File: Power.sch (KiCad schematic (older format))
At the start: 0 parts

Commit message: Completed LED Driver Video + Power Module
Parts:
- added C? (x2): C, ~, symbol C
- added F? (x4): FUSE, ~, symbol FUSE
- added L? (x2): INDUCTOR, ~, symbol INDUCTOR
- added P?: CONN_12X2, symbol CONN_12X2
- added R?: R, ~, symbol R
- added SW?: SWITCH_INV, ~, symbol SWITCH_INV
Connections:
- net labels added: +12P, +12V, +3.3V, +5V, -12P, -12V, GND
- wire segments 0 -> 36
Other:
- note added: "CONFIRM DGND AND GND CONNECTIONS BEFORE LAYOUT"

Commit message: Fan Module Update
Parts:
- removed F? (x4): FUSE, ~, symbol FUSE
- added TH? (x4): THERMISTOR, ~, symbol THERMISTOR
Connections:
- net labels added: +12C
- wire segments 36 -> 37
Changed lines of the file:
@@
 	1    0    0    -1
 $EndComp
-Text Notes 1000 2700 0    60   ~ 0
+Text Notes 1050 2350 0    60   ~ 0
 CONFIRM DGND AND GND CONNECTIONS BEFORE LAYOUT
 $Comp
@@
 $EndComp
 $Comp
-L FUSE F?
-U 1 1 52F68298
-P 3700 3350
-F 0 "F?" H 3800 3400 40  0000 C CNN
-F 1 "FUSE" H 3600 3300 40  0000 C CNN
-F 2 "~" H 3700 3350 60  0000 C CNN
-F 3 "~" H 3700 3350 60  0000 C CNN
-	1    3700 3350
-	1    0    0    -1
-$EndComp
-$Comp
-L FUSE F?
-U 1 1 52F682A5
-P 4350 3550
-F 0 "F?" H 4450 3600 40  0000 C CNN
-F 1 "FUSE" H 4250 3500 40  0000 C CNN
-F 2 "~" H 4350 3550 60  0000 C CNN
-F 3 "~" H 4350 3550 60  0000 C CNN
-	1    4350 3550
-	1    0    0    -1
-$EndComp
-$Comp
-L FUSE F?
-U 1 1 52F682AB
-P 5000 3750
-F 0 "F?" H 5100 3800 40  0000 C CNN
-F 1 "FUSE" H 4900 3700 40  0000 C CNN
-F 2 "~" H 5000 3750 60  0000 C CNN
-F 3 "~" H 5000 3750 60  0000 C CNN
-	1    5000 3750
-	1    0    0    -1
-$EndComp
-$Comp
-L FUSE F?
-U 1 1 52F682B1
-P 5700 3950
-F 0 "F?" H 5800 4000 40  0000 C CNN
-F 1 "FUSE" H 5600 3900 40  0000 C CNN
-F 2 "~" H 5700 3950 60  0000 C CNN
-F 3 "~" H 5700 3950 60  0000 C CNN
-	1    5700 3950
-	1    0    0    -1
-$EndComp
-$Comp
 L SWITCH_INV SW?
 U 1 1 52F682B9
@@
 Wire Wire Line
 	10450 3650 10450 3450
+$Comp
+L +12C #PWR?
+U 1 1 52FA4EC0
+P 3250 2750
+F 0 "#PWR?" H 3250 2720 30  0001 C CNN
+F 1 "+12C" H 3250 2860 40  0000 C CNN
+F 2 "" H 3250 2750 60  0000 C CNN
+F 3 "" H 3250 2750 60  0000 C CNN
+	1    3250 2750
+	1    0    0    -1
+$EndComp
+Wire Wire Line
+	3250 2750 3250 3750
+Connection ~ 3250 3750
+$Comp
+L THERMISTOR TH?
+U 1 1 52FA5A15
+P 3700 3350
+F 0 "TH?" V 3800 3400 50  0000 C CNN
+F 1 "THERMISTOR" V 3600 3350 50  0000 C CNN
+F 2 "~" H 3700 3350 60  0000 C CNN
+F 3 "~" H 3700 3350 60  0000 C CNN
+	1    3700 3350
+	0    -1   -1   0
+$EndComp
+$Comp
+L THERMISTOR TH?
+U 1 1 52FA5A22
+P 4350 3550
+F 0 "TH?" V 4450 3600 50  0000 C CNN
+F 1 "THERMISTOR" V 4250 3550 50  0000 C CNN
+F 2 "~" H 4350 3550 60  0000 C CNN
+F 3 "~" H 4350 3550 60  0000 C CNN
+	1    4350 3550
+	0    -1   -1   0
+$EndComp
+$Comp
+L THERMISTOR TH?
+U 1 1 52FA5A28
+P 5000 3750
+F 0 "TH?" V 5100 3800 50  0000 C CNN
+F 1 "THERMISTOR" V 4900 3750 50  0000 C CNN
+F 2 "~" H 5000 3750 60  0000 C CNN
+F 3 "~" H 5000 3750 60  0000 C CNN
+	1    5000 3750
+	0    -1   -1   0
+$EndComp
+$Comp
+L THERMISTOR TH?
+U 1 1 52FA5A2E
+P 5700 3950
+F 0 "TH?" V 5800 4000 50  0000 C CNN
+F 1 "THERMISTOR" V 5600 3950 50  0000 C CNN
+F 2 "~" H 5700 3950 60  0000 C CNN
+F 3 "~" H 5700 3950 60  0000 C CNN
+	1    5700 3950
+	0    -1   -1   0
+$EndComp
 $EndSCHEMATC

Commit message: Started Layout Outline.  Completed other schem videos
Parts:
- added C?: C, ~, symbol C
- added L?: INDUCTOR, ~, symbol INDUCTOR
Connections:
- net +3.3V: no longer TH?.2
- net +5V: now also C?.1, L?.2; no longer TH?.2
- net GND: now also C?.2
- new net +3.3VP: TH?.2
- new net +5P: L?.1, TH?.2
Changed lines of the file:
@@
 $Descr A4 11693 8268
 encoding utf-8
-Sheet 4 9
+Sheet 3 9
 Title ""
-Date "11 feb 2014"
+Date "17 feb 2014"
 Rev ""
 Comp ""
@@
 L +5V #PWR?
 U 1 1 52F67F60
-P 5250 2750
-F 0 "#PWR?" H 5250 2840 20  0001 C CNN
-F 1 "+5V" H 5250 2840 30  0000 C CNN
-F 2 "" H 5250 2750 60  0000 C CNN
-F 3 "" H 5250 2750 60  0000 C CNN
-	1    5250 2750
-	1    0    0    -1
-$EndComp
-$Comp
-L +3.3V #PWR?
-U 1 1 52F68100
-P 4650 2750
-F 0 "#PWR?" H 4650 2710 30  0001 C CNN
-F 1 "+3.3V" H 4650 2860 30  0000 C CNN
-F 2 "" H 4650 2750 60  0000 C CNN
-F 3 "" H 4650 2750 60  0000 C CNN
-	1    4650 2750
+P 10450 2000
+F 0 "#PWR?" H 10450 2090 20  0001 C CNN
+F 1 "+5V" H 10450 2090 30  0000 C CNN
+F 2 "" H 10450 2000 60  0000 C CNN
+F 3 "" H 10450 2000 60  0000 C CNN
+	1    10450 2000
 	1    0    0    -1
 $EndComp
@@
 	9750 5050 9750 4950
 Wire Wire Line
-	9750 4550 9750 4150
+	9750 4150 9750 4550
 Wire Wire Line
 	9150 3650 10450 3650
@@
 	0    -1   -1   0
 $EndComp
+$Comp
+L +5P #PWR?
+U 1 1 530231B7
+P 5250 2750
+F 0 "#PWR?" H 5250 2880 20  0001 C CNN
+F 1 "+5P" H 5250 2850 30  0000 C CNN
+F 2 "" H 5250 2750 60  0000 C CNN
+F 3 "" H 5250 2750 60  0000 C CNN
+	1    5250 2750
+	1    0    0    -1
+$EndComp
+$Comp
+L +5P #PWR?
+U 1 1 530231D8
+P 8050 2000
+F 0 "#PWR?" H 8050 2130 20  0001 C CNN
+F 1 "+5P" H 8050 2100 30  0000 C CNN
+F 2 "" H 8050 2000 60  0000 C CNN
+F 3 "" H 8050 2000 60  0000 C CNN
+	1    8050 2000
+	1    0    0    -1
+$EndComp
+$Comp
+L INDUCTOR L?
+U 1 1 530231DE
+P 8850 2300
+F 0 "L?" V 8800 2300 40  0000 C CNN
+F 1 "INDUCTOR" V 8950 2300 40  0000 C CNN
+F 2 "~" H 8850 2300 60  0000 C CNN
+F 3 "~" H 8850 2300 60  0000 C CNN
+	1    8850 2300
+	0    -1   -1   0
+$EndComp
+$Comp
+L C C?
+U 1 1 530231E4
+P 9750 2600
+F 0 "C?" H 9750 2700 40  0000 L CNN
+F 1 "C" H 9756 2515 40  0000 L CNN
+F 2 "~" H 9788 2450 30  0000 C CNN
+F 3 "~" H 9750 2600 60  0000 C CNN
+	1    9750 2600
+	1    0    0    -1
+$EndComp
+Wire Wire Line
+	9150 2300 10450 2300
+$Comp
+L GND #PWR?
+U 1 1 530231EC
+P 9750 3150
+F 0 "#PWR?" H 9750 3150 30  0001 C CNN
+F 1 "GND" H 9750 3080 30  0001 C CNN
+F 2 "" H 9750 3150 60  0000 C CNN
+F 3 "" H 9750 3150 60  0000 C CNN
+	1    9750 3150
+	1    0    0    -1
+$EndComp
+Wire Wire Line
+	9750 2800 9750 3150
+Wire Wire Line
+	8550 2300 8050 2300
+Connection ~ 9750 2300
+Wire Wire Line
+	9750 2300 9750 2400
+Wire Wire Line
+	10450 2300 10450 2000
+Wire Wire Line
+	8050 2300 8050 2000
+$Comp
+L +3.3VP #PWR?
+U 1 1 53023523
+P 4650 2750
+F 0 "#PWR?" H 4700 2780 20  0001 C CNN
+F 1 "+3.3VP" H 4650 2840 30  0000 C CNN
+F 2 "" H 4650 2750 60  0000 C CNN
+F 3 "" H 4650 2750 60  0000 C CNN
+	1    4650 2750
+	1    0    0    -1
+$EndComp
 $EndSCHEMATC

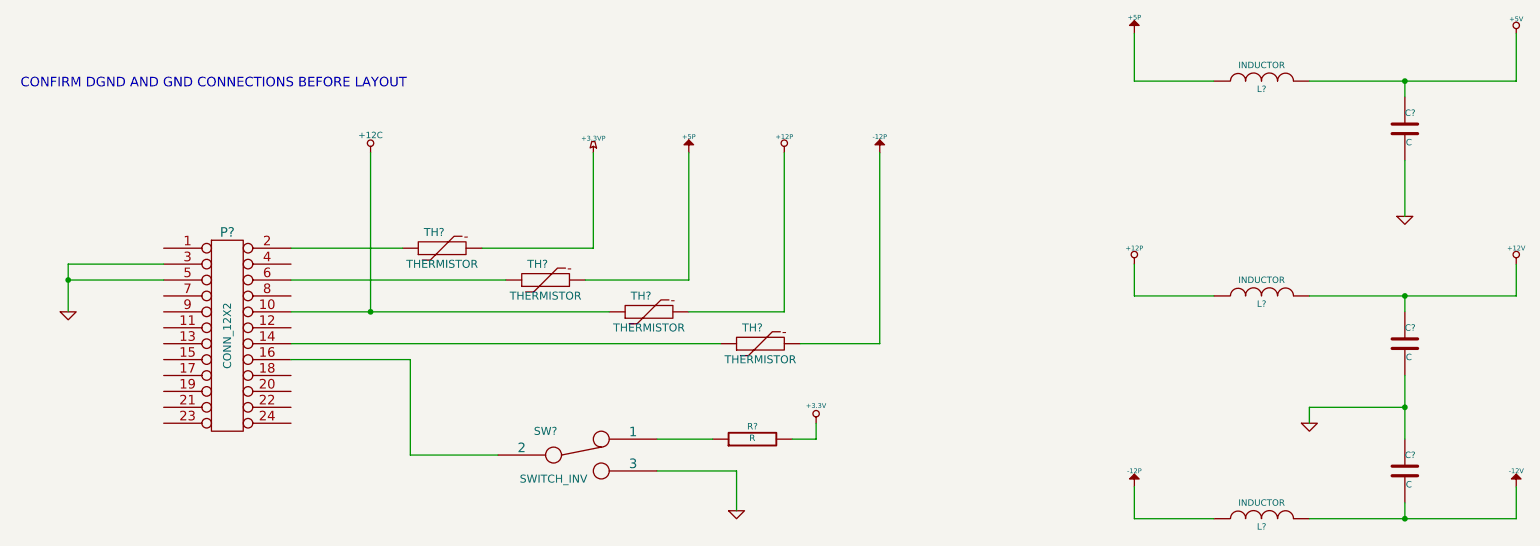
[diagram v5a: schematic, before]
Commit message: started associating relay parts
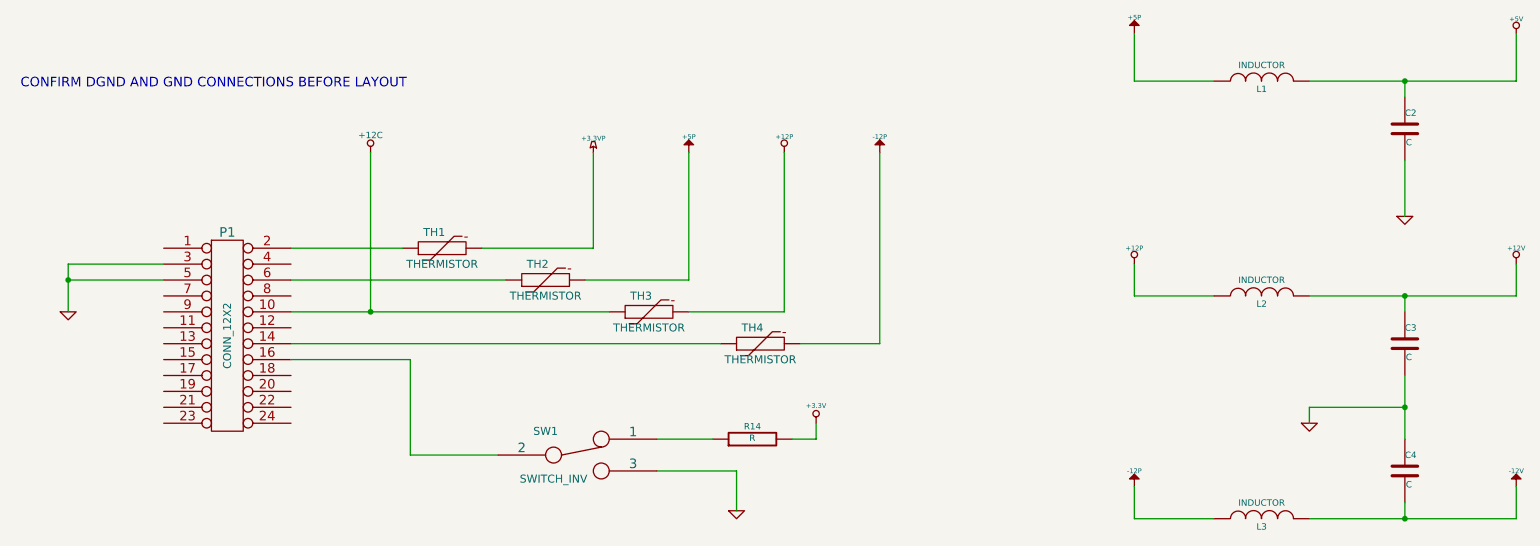
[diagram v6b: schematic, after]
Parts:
- gave numbers to parts that had none: 13
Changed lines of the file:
@@
 Sheet 3 9
 Title ""
-Date "17 feb 2014"
+Date "20 feb 2014"
 Rev ""
 Comp ""
@@
 $EndDescr
 $Comp
-L CONN_12X2 P?
+L CONN_12X2 P1
 U 1 1 52F67DB2
 P 2350 3900
-F 0 "P?" H 2350 4550 60  0000 C CNN
+F 0 "P1" H 2350 4550 60  0000 C CNN
 F 1 "CONN_12X2" V 2350 3900 50  0000 C CNN
 F 2 "" H 2350 3900 60  0000 C CNN
@@
 $EndComp
 $Comp
-L +3.3V #PWR?
+L +3.3V #PWR010
 U 1 1 52F67DC1
 P 6050 4450
-F 0 "#PWR?" H 6050 4410 30  0001 C CNN
+F 0 "#PWR010" H 6050 4410 30  0001 C CNN
 F 1 "+3.3V" H 6050 4560 30  0000 C CNN
 F 2 "" H 6050 4450 60  0000 C CNN
@@
 $EndComp
 $Comp
-L GND #PWR?
+L GND #PWR011
 U 1 1 52F67DD1
 P 1350 3750
-F 0 "#PWR?" H 1350 3750 30  0001 C CNN
+F 0 "#PWR011" H 1350 3750 30  0001 C CNN
 F 1 "GND" H 1350 3680 30  0001 C CNN
 F 2 "" H 1350 3750 60  0000 C CNN
@@
 CONFIRM DGND AND GND CONNECTIONS BEFORE LAYOUT
 $Comp
-L +5V #PWR?
+L +5V #PWR012
 U 1 1 52F67F60
 P 10450 2000
-F 0 "#PWR?" H 10450 2090 20  0001 C CNN
+F 0 "#PWR012" H 10450 2090 20  0001 C CNN
 F 1 "+5V" H 10450 2090 30  0000 C CNN
 F 2 "" H 10450 2000 60  0000 C CNN
@@
 $EndComp
 $Comp
-L SWITCH_INV SW?
+L SWITCH_INV SW1
 U 1 1 52F682B9
 P 4550 4650
-F 0 "SW?" H 4350 4800 50  0000 C CNN
+F 0 "SW1" H 4350 4800 50  0000 C CNN
 F 1 "SWITCH_INV" H 4400 4500 50  0000 C CNN
 F 2 "~" H 4550 4650 60  0000 C CNN
@@
 $EndComp
 $Comp
-L +12P #PWR?
+L +12P #PWR013
 U 1 1 52F682C8
 P 5850 2750
-F 0 "#PWR?" H 5850 2720 30  0001 C CNN
+F 0 "#PWR013" H 5850 2720 30  0001 C CNN
 F 1 "+12P" H 5850 2850 30  0000 C CNN
 F 2 "" H 5850 2750 60  0000 C CNN
@@
 $EndComp
 $Comp
-L -12P #PWR?
+L -12P #PWR014
 U 1 1 52F68B13
 P 6450 2750
-F 0 "#PWR?" H 6450 2880 20  0001 C CNN
+F 0 "#PWR014" H 6450 2880 20  0001 C CNN
 F 1 "-12P" H 6450 2850 30  0000 C CNN
 F 2 "" H 6450 2750 60  0000 C CNN
@@
 	3500 4050 2750 4050
 $Comp
-L GND #PWR?
+L GND #PWR015
 U 1 1 52F68F28
 P 5550 5000
-F 0 "#PWR?" H 5550 5000 30  0001 C CNN
+F 0 "#PWR015" H 5550 5000 30  0001 C CNN
 F 1 "GND" H 5550 4930 30  0001 C CNN
 F 2 "" H 5550 5000 60  0000 C CNN
@@
 	5550 4750 5550 5000
 $Comp
-L R R?
+L R R14
 U 1 1 52F68F4E
 P 5650 4550
-F 0 "R?" V 5730 4550 40  0000 C CNN
+F 0 "R14" V 5730 4550 40  0000 C CNN
 F 1 "R" V 5657 4551 40  0000 C CNN
 F 2 "~" V 5580 4550 30  0000 C CNN
@@
 	6050 4550 6050 4450
 $Comp
-L +12P #PWR?
+L +12P #PWR016
 U 1 1 52F68F88
 P 8050 3450
-F 0 "#PWR?" H 8050 3420 30  0001 C CNN
+F 0 "#PWR016" H 8050 3420 30  0001 C CNN
 F 1 "+12P" H 8050 3550 30  0000 C CNN
 F 2 "" H 8050 3450 60  0000 C CNN
@@
 $EndComp
 $Comp
-L -12P #PWR?
+L -12P #PWR017
 U 1 1 52F68F8E
 P 8050 4850
-F 0 "#PWR?" H 8050 4980 20  0001 C CNN
+F 0 "#PWR017" H 8050 4980 20  0001 C CNN
 F 1 "-12P" H 8050 4950 30  0000 C CNN
 F 2 "" H 8050 4850 60  0000 C CNN
@@
 $EndComp
 $Comp
-L INDUCTOR L?
+L INDUCTOR L2
 U 1 1 52F68FA0
 P 8850 3650
-F 0 "L?" V 8800 3650 40  0000 C CNN
+F 0 "L2" V 8800 3650 40  0000 C CNN
 F 1 "INDUCTOR" V 8950 3650 40  0000 C CNN
 F 2 "~" H 8850 3650 60  0000 C CNN
@@
 $EndComp
 $Comp
-L INDUCTOR L?
+L INDUCTOR L3
 U 1 1 52F68FAD
 P 8850 5050
-F 0 "L?" V 8800 5050 40  0000 C CNN
+F 0 "L3" V 8800 5050 40  0000 C CNN
 F 1 "INDUCTOR" V 8950 5050 40  0000 C CNN
 F 2 "~" H 8850 5050 60  0000 C CNN
@@
 $EndComp
 $Comp
-L C C?
+L C C3
 U 1 1 52F68FC9
 P 9750 3950
-F 0 "C?" H 9750 4050 40  0000 L CNN
+F 0 "C3" H 9750 4050 40  0000 L CNN
 F 1 "C" H 9756 3865 40  0000 L CNN
 F 2 "~" H 9788 3800 30  0000 C CNN
@@
 $EndComp
 $Comp
-L C C?
+L C C4
 U 1 1 52F68FD6
 P 9750 4750
-F 0 "C?" H 9750 4850 40  0000 L CNN
+F 0 "C4" H 9750 4850 40  0000 L CNN
 F 1 "C" H 9756 4665 40  0000 L CNN
 F 2 "~" H 9788 4600 30  0000 C CNN
@@
 	9150 3650 10450 3650
 $Comp
-L GND #PWR?
+L GND #PWR018
 U 1 1 52F6902C
 P 9150 4450
-F 0 "#PWR?" H 9150 4450 30  0001 C CNN
+F 0 "#PWR018" H 9150 4450 30  0001 C CNN
 F 1 "GND" H 9150 4380 30  0001 C CNN
 F 2 "" H 9150 4450 60  0000 C CNN
@@
 	8050 3650 8050 3450
 $Comp
-L +12V #PWR?
+L +12V #PWR019
 U 1 1 52F690A0
 P 10450 3450
-F 0 "#PWR?" H 10450 3400 20  0001 C CNN
+F 0 "#PWR019" H 10450 3400 20  0001 C CNN
 F 1 "+12V" H 10450 3550 30  0000 C CNN
 F 2 "" H 10450 3450 60  0000 C CNN
@@
 Connection ~ 9750 3650
 $Comp
-L -12V #PWR?
+L -12V #PWR020
 U 1 1 52F690D4
 P 10450 4850
-F 0 "#PWR?" H 10450 4980 20  0001 C CNN
+F 0 "#PWR020" H 10450 4980 20  0001 C CNN
 F 1 "-12V" H 10450 4950 30  0000 C CNN
 F 2 "" H 10450 4850 60  0000 C CNN
@@
 	10450 3650 10450 3450
 $Comp
-L +12C #PWR?
+L +12C #PWR021
 U 1 1 52FA4EC0
 P 3250 2750
-F 0 "#PWR?" H 3250 2720 30  0001 C CNN
+F 0 "#PWR021" H 3250 2720 30  0001 C CNN
 F 1 "+12C" H 3250 2860 40  0000 C CNN
 F 2 "" H 3250 2750 60  0000 C CNN
@@
 Connection ~ 3250 3750
 $Comp
-L THERMISTOR TH?
+L THERMISTOR TH1
 U 1 1 52FA5A15
 P 3700 3350
-F 0 "TH?" V 3800 3400 50  0000 C CNN
+F 0 "TH1" V 3800 3400 50  0000 C CNN
 F 1 "THERMISTOR" V 3600 3350 50  0000 C CNN
 F 2 "~" H 3700 3350 60  0000 C CNN
@@
 $EndComp
 $Comp
-L THERMISTOR TH?
+L THERMISTOR TH2
 U 1 1 52FA5A22
 P 4350 3550
-F 0 "TH?" V 4450 3600 50  0000 C CNN
+F 0 "TH2" V 4450 3600 50  0000 C CNN
 F 1 "THERMISTOR" V 4250 3550 50  0000 C CNN
 F 2 "~" H 4350 3550 60  0000 C CNN
@@
 $EndComp
 $Comp
-L THERMISTOR TH?
+L THERMISTOR TH3
 U 1 1 52FA5A28
 P 5000 3750
-F 0 "TH?" V 5100 3800 50  0000 C CNN
+F 0 "TH3" V 5100 3800 50  0000 C CNN
 F 1 "THERMISTOR" V 4900 3750 50  0000 C CNN
 F 2 "~" H 5000 3750 60  0000 C CNN
@@
 $EndComp
 $Comp
-L THERMISTOR TH?
+L THERMISTOR TH4
 U 1 1 52FA5A2E
 P 5700 3950
-F 0 "TH?" V 5800 4000 50  0000 C CNN
+F 0 "TH4" V 5800 4000 50  0000 C CNN
 F 1 "THERMISTOR" V 5600 3950 50  0000 C CNN
 F 2 "~" H 5700 3950 60  0000 C CNN
@@
 $EndComp
 $Comp
-L +5P #PWR?
+L +5P #PWR13
 U 1 1 530231B7
 P 5250 2750
-F 0 "#PWR?" H 5250 2880 20  0001 C CNN
+F 0 "#PWR13" H 5250 2880 20  0001 C CNN
 F 1 "+5P" H 5250 2850 30  0000 C CNN
 F 2 "" H 5250 2750 60  0000 C CNN
@@
 $EndComp
 $Comp
-L +5P #PWR?
+L +5P #PWR18
 U 1 1 530231D8
 P 8050 2000
-F 0 "#PWR?" H 8050 2130 20  0001 C CNN
+F 0 "#PWR18" H 8050 2130 20  0001 C CNN
 F 1 "+5P" H 8050 2100 30  0000 C CNN
 F 2 "" H 8050 2000 60  0000 C CNN
@@
 $EndComp
 $Comp
-L INDUCTOR L?
+L INDUCTOR L1
 U 1 1 530231DE
 P 8850 2300
-F 0 "L?" V 8800 2300 40  0000 C CNN
+F 0 "L1" V 8800 2300 40  0000 C CNN
 F 1 "INDUCTOR" V 8950 2300 40  0000 C CNN
 F 2 "~" H 8850 2300 60  0000 C CNN
@@
 $EndComp
 $Comp
-L C C?
+L C C2
 U 1 1 530231E4
 P 9750 2600
-F 0 "C?" H 9750 2700 40  0000 L CNN
+F 0 "C2" H 9750 2700 40  0000 L CNN
 F 1 "C" H 9756 2515 40  0000 L CNN
 F 2 "~" H 9788 2450 30  0000 C CNN
@@
 	9150 2300 10450 2300
 $Comp
-L GND #PWR?
+L GND #PWR022
 U 1 1 530231EC
 P 9750 3150
-F 0 "#PWR?" H 9750 3150 30  0001 C CNN
+F 0 "#PWR022" H 9750 3150 30  0001 C CNN
 F 1 "GND" H 9750 3080 30  0001 C CNN
 F 2 "" H 9750 3150 60  0000 C CNN
@@
 	8050 2300 8050 2000
 $Comp
-L +3.3VP #PWR?
+L +3.3VP #PWR023
 U 1 1 53023523
 P 4650 2750
-F 0 "#PWR?" H 4700 2780 20  0001 C CNN
+F 0 "#PWR023" H 4700 2780 20  0001 C CNN
 F 1 "+3.3VP" H 4650 2840 30  0000 C CNN
 F 2 "" H 4650 2750 60  0000 C CNN

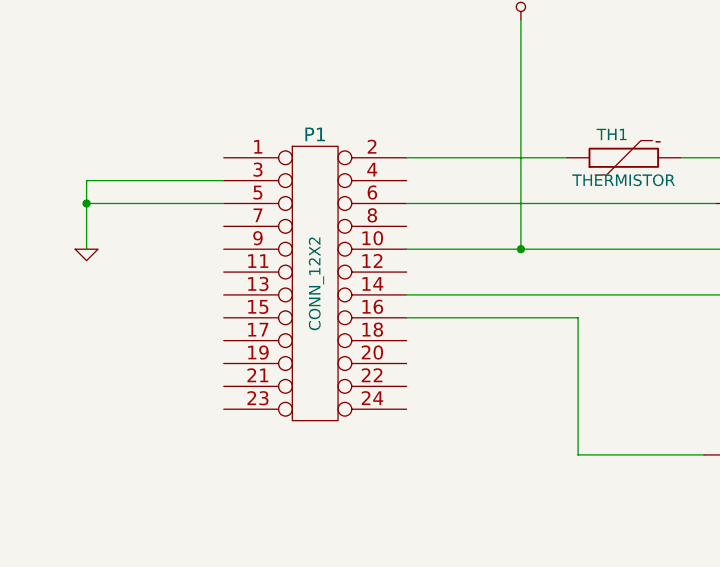
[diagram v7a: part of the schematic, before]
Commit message: Completed terminal block placement and footprints
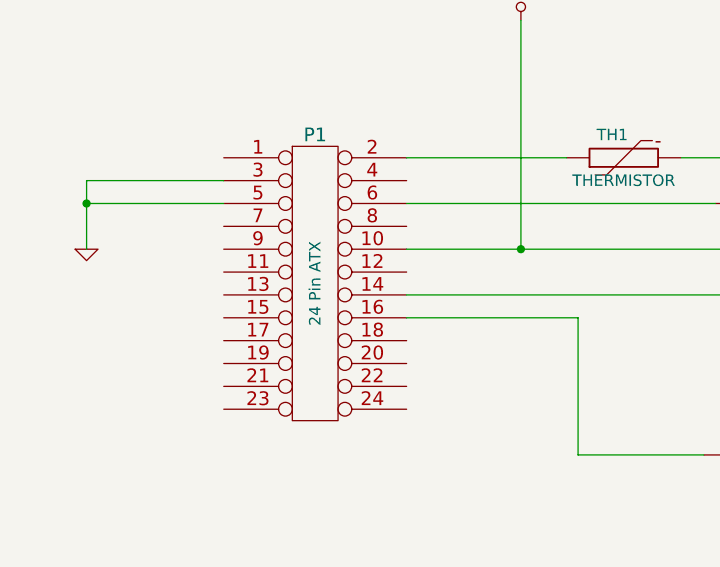
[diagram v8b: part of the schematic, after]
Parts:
- P1: value CONN_12X2 -> 24 Pin ATX; MFG Name (none) -> Molex; Part Number (none) -> 39-30-1240
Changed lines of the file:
@@
 Sheet 3 9
 Title ""
-Date "23 feb 2014"
+Date "2 mar 2014"
 Rev ""
 Comp ""
@@
 P 2350 3900
 F 0 "P1" H 2350 4550 60  0000 C CNN
-F 1 "CONN_12X2" V 2350 3900 50  0000 C CNN
+F 1 "24 Pin ATX" V 2350 3900 50  0000 C CNN
 F 2 "" H 2350 3900 60  0000 C CNN
 F 3 "" H 2350 3900 60  0000 C CNN
+F 4 "39-30-1240" H 2350 3900 60  0001 C CNN "Part Number"
+F 5 "Molex" H 2350 3900 60  0001 C CNN "MFG Name"
 	1    2350 3900
 	1    0    0    -1
 $EndComp
 $Comp
-L +3.3V #PWR27
+L +3.3V #PWR021
 U 1 1 52F67DC1
 P 6050 4450
-F 0 "#PWR27" H 6050 4410 30  0001 C CNN
+F 0 "#PWR021" H 6050 4410 30  0001 C CNN
 F 1 "+3.3V" H 6050 4560 30  0000 C CNN
 F 2 "" H 6050 4450 60  0000 C CNN
@@
 $EndComp
 $Comp
-L GND #PWR21
+L GND #PWR022
 U 1 1 52F67DD1
 P 1350 3750
-F 0 "#PWR21" H 1350 3750 30  0001 C CNN
+F 0 "#PWR022" H 1350 3750 30  0001 C CNN
 F 1 "GND" H 1350 3680 30  0001 C CNN
 F 2 "" H 1350 3750 60  0000 C CNN
@@
 CONFIRM DGND AND GND CONNECTIONS BEFORE LAYOUT
 $Comp
-L +5V #PWR34
+L +5V #PWR023
 U 1 1 52F67F60
 P 10450 2000
-F 0 "#PWR34" H 10450 2090 20  0001 C CNN
+F 0 "#PWR023" H 10450 2090 20  0001 C CNN
 F 1 "+5V" H 10450 2090 30  0000 C CNN
 F 2 "" H 10450 2000 60  0000 C CNN
@@
 $EndComp
 $Comp
-L +12P #PWR26
+L +12P #PWR024
 U 1 1 52F682C8
 P 5850 2750
-F 0 "#PWR26" H 5850 2720 30  0001 C CNN
+F 0 "#PWR024" H 5850 2720 30  0001 C CNN
 F 1 "+12P" H 5850 2850 30  0000 C CNN
 F 2 "" H 5850 2750 60  0000 C CNN
@@
 $EndComp
 $Comp
-L -12P #PWR28
+L -12P #PWR025
 U 1 1 52F68B13
 P 6450 2750
-F 0 "#PWR28" H 6450 2880 20  0001 C CNN
+F 0 "#PWR025" H 6450 2880 20  0001 C CNN
 F 1 "-12P" H 6450 2850 30  0000 C CNN
 F 2 "" H 6450 2750 60  0000 C CNN
@@
 	3500 4050 2750 4050
 $Comp
-L GND #PWR25
+L GND #PWR026
 U 1 1 52F68F28
 P 5550 5000
-F 0 "#PWR25" H 5550 5000 30  0001 C CNN
+F 0 "#PWR026" H 5550 5000 30  0001 C CNN
 F 1 "GND" H 5550 4930 30  0001 C CNN
 F 2 "" H 5550 5000 60  0000 C CNN
@@
 	6050 4550 6050 4450
 $Comp
-L +12P #PWR30
+L +12P #PWR027
 U 1 1 52F68F88
 P 8050 3450
-F 0 "#PWR30" H 8050 3420 30  0001 C CNN
+F 0 "#PWR027" H 8050 3420 30  0001 C CNN
 F 1 "+12P" H 8050 3550 30  0000 C CNN
 F 2 "" H 8050 3450 60  0000 C CNN
@@
 $EndComp
 $Comp
-L -12P #PWR31
+L -12P #PWR028
 U 1 1 52F68F8E
 P 8050 4850
-F 0 "#PWR31" H 8050 4980 20  0001 C CNN
+F 0 "#PWR028" H 8050 4980 20  0001 C CNN
 F 1 "-12P" H 8050 4950 30  0000 C CNN
 F 2 "" H 8050 4850 60  0000 C CNN
@@
 	9150 3650 10450 3650
 $Comp
-L GND #PWR32
+L GND #PWR029
 U 1 1 52F6902C
 P 9150 4450
-F 0 "#PWR32" H 9150 4450 30  0001 C CNN
+F 0 "#PWR029" H 9150 4450 30  0001 C CNN
 F 1 "GND" H 9150 4380 30  0001 C CNN
 F 2 "" H 9150 4450 60  0000 C CNN
@@
 	8050 3650 8050 3450
 $Comp
-L +12V #PWR35
+L +12V #PWR030
 U 1 1 52F690A0
 P 10450 3450
-F 0 "#PWR35" H 10450 3400 20  0001 C CNN
+F 0 "#PWR030" H 10450 3400 20  0001 C CNN
 F 1 "+12V" H 10450 3550 30  0000 C CNN
 F 2 "" H 10450 3450 60  0000 C CNN
@@
 Connection ~ 9750 3650
 $Comp
-L -12V #PWR36
+L -12V #PWR031
 U 1 1 52F690D4
 P 10450 4850
-F 0 "#PWR36" H 10450 4980 20  0001 C CNN
+F 0 "#PWR031" H 10450 4980 20  0001 C CNN
 F 1 "-12V" H 10450 4950 30  0000 C CNN
 F 2 "" H 10450 4850 60  0000 C CNN
@@
 	10450 3650 10450 3450
 $Comp
-L +12C #PWR22
+L +12C #PWR032
 U 1 1 52FA4EC0
 P 3250 2750
-F 0 "#PWR22" H 3250 2720 30  0001 C CNN
+F 0 "#PWR032" H 3250 2720 30  0001 C CNN
 F 1 "+12C" H 3250 2860 40  0000 C CNN
 F 2 "" H 3250 2750 60  0000 C CNN
@@
 	9150 2300 10450 2300
 $Comp
-L GND #PWR33
+L GND #PWR033
 U 1 1 530231EC
 P 9750 3150
-F 0 "#PWR33" H 9750 3150 30  0001 C CNN
+F 0 "#PWR033" H 9750 3150 30  0001 C CNN
 F 1 "GND" H 9750 3080 30  0001 C CNN
 F 2 "" H 9750 3150 60  0000 C CNN
@@
 	8050 2300 8050 2000
 $Comp
-L +3.3VP #PWR23
+L +3.3VP #PWR034
 U 1 1 53023523
 P 4650 2750
-F 0 "#PWR23" H 4700 2780 20  0001 C CNN
+F 0 "#PWR034" H 4700 2780 20  0001 C CNN
 F 1 "+3.3VP" H 4650 2840 30  0000 C CNN
 F 2 "" H 4650 2750 60  0000 C CNN
